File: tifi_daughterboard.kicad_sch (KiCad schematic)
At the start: 20 parts, among them J1 SSW-110-23-F-D, J2 SSW-110-23-F-D, J3 SM04B-SRSS-TB(LF)(SN), J4 SSW-103-02-T-S-RA, Q1 BSS138LT1G, U1 SGP40-D-R4, U2 SHT40-AD1B-R3

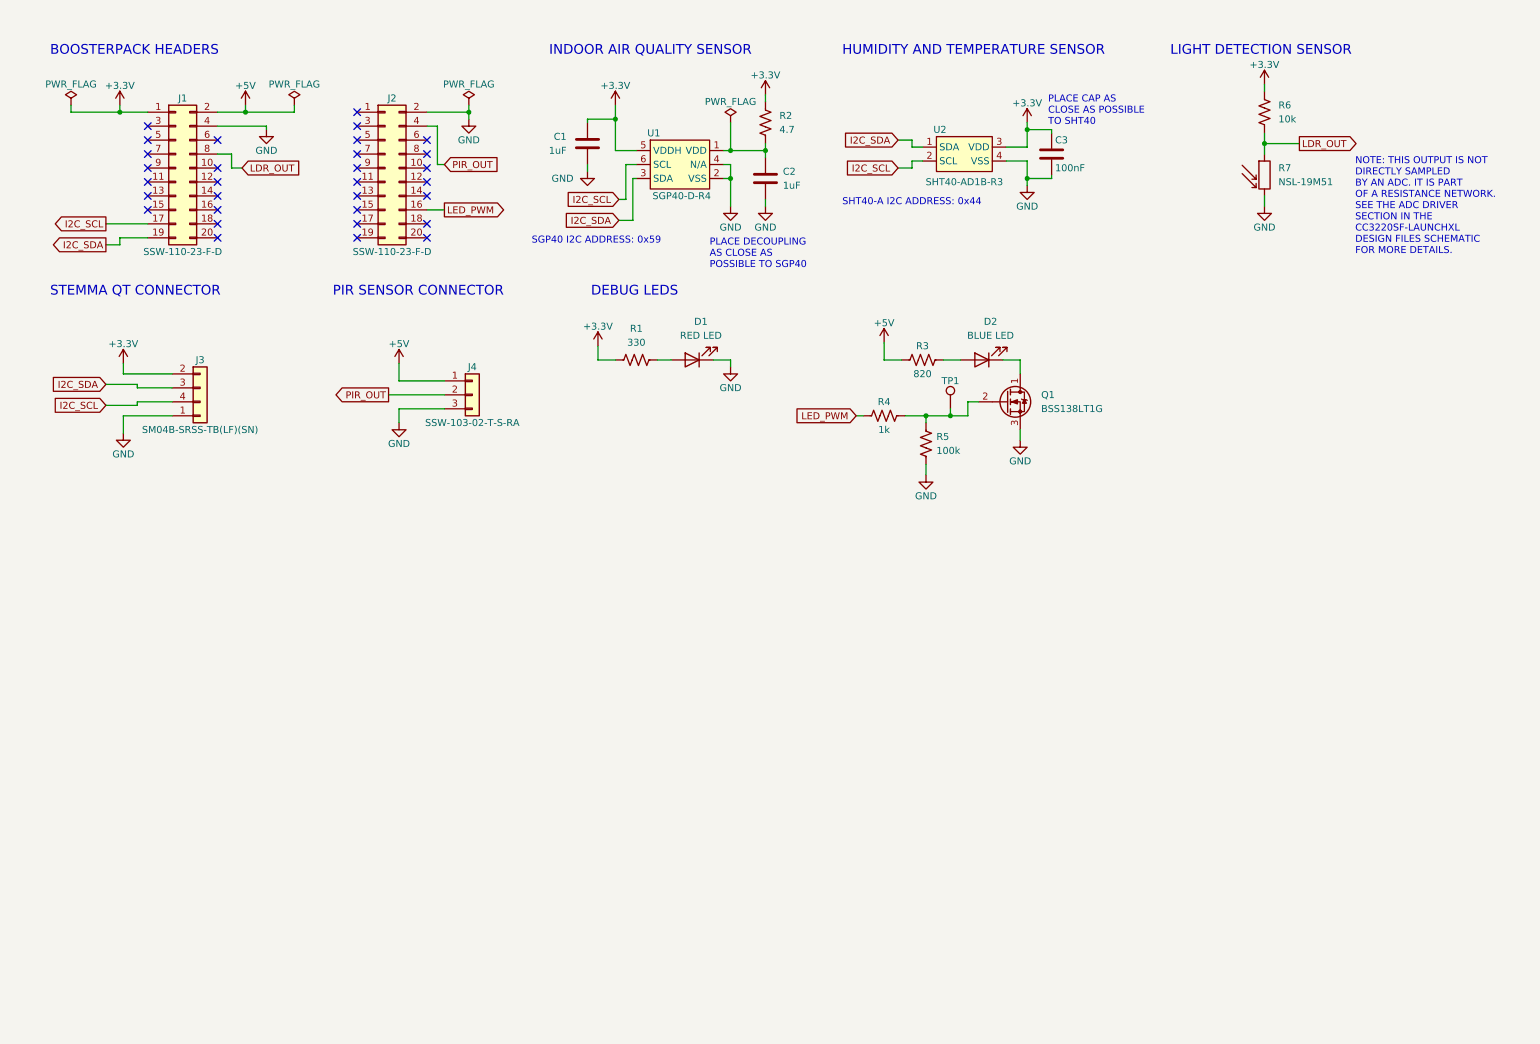
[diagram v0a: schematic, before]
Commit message: Add TVS diodes to connectors.
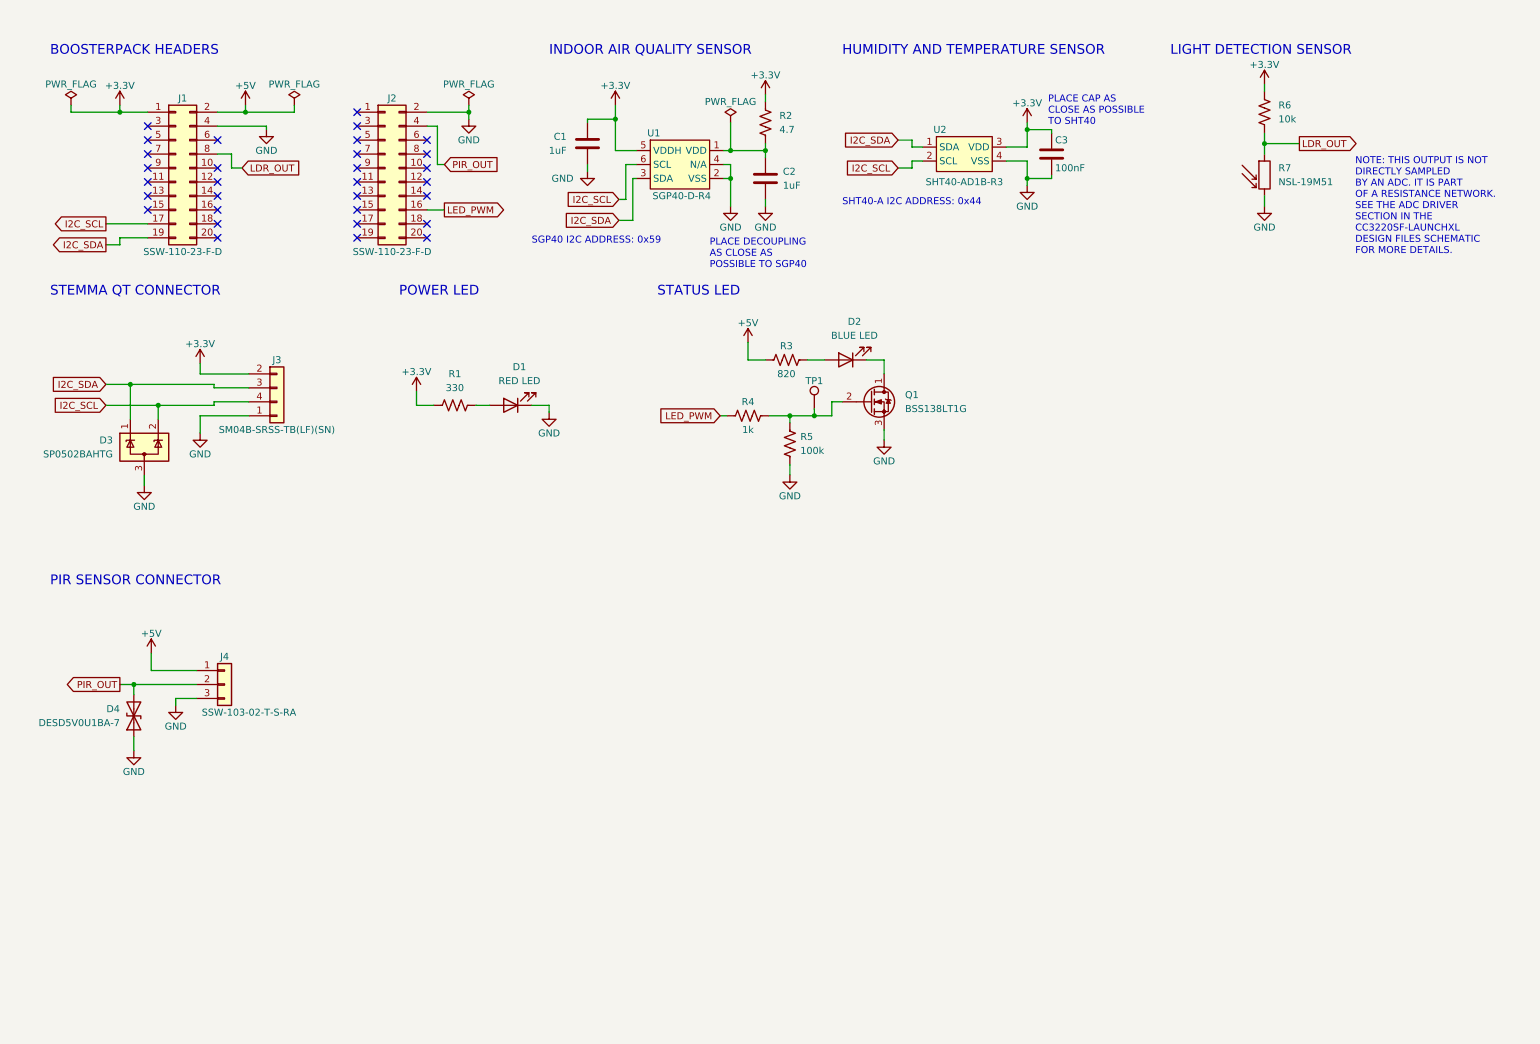
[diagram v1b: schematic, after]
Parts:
- added D3: SP0502BAHTG, Package_TO_SOT_SMD:SOT-23, symbol Power_Protection:SP0502BAHT
- added D4: DESD5V0U1BA-7, TiFi Footprints:D_SOD-323, symbol Device:D_TVS
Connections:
- net GND: now also D3.3 (A), D4.1 (A1)
- net I2C_SCL: now also D3.2 (K)
- net I2C_SDA: now also D3.1 (K)
- net PIR_OUT: now also D4.2 (A2)
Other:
- note added: "POWER LED"
- note added: "STATUS LED"
- note removed: "DEBUG LEDS"
- moved on the sheet: D1, D2, J3, J4, Q1, R1, R3, R4, R5, TP1

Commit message: Add optional I2C pullups.
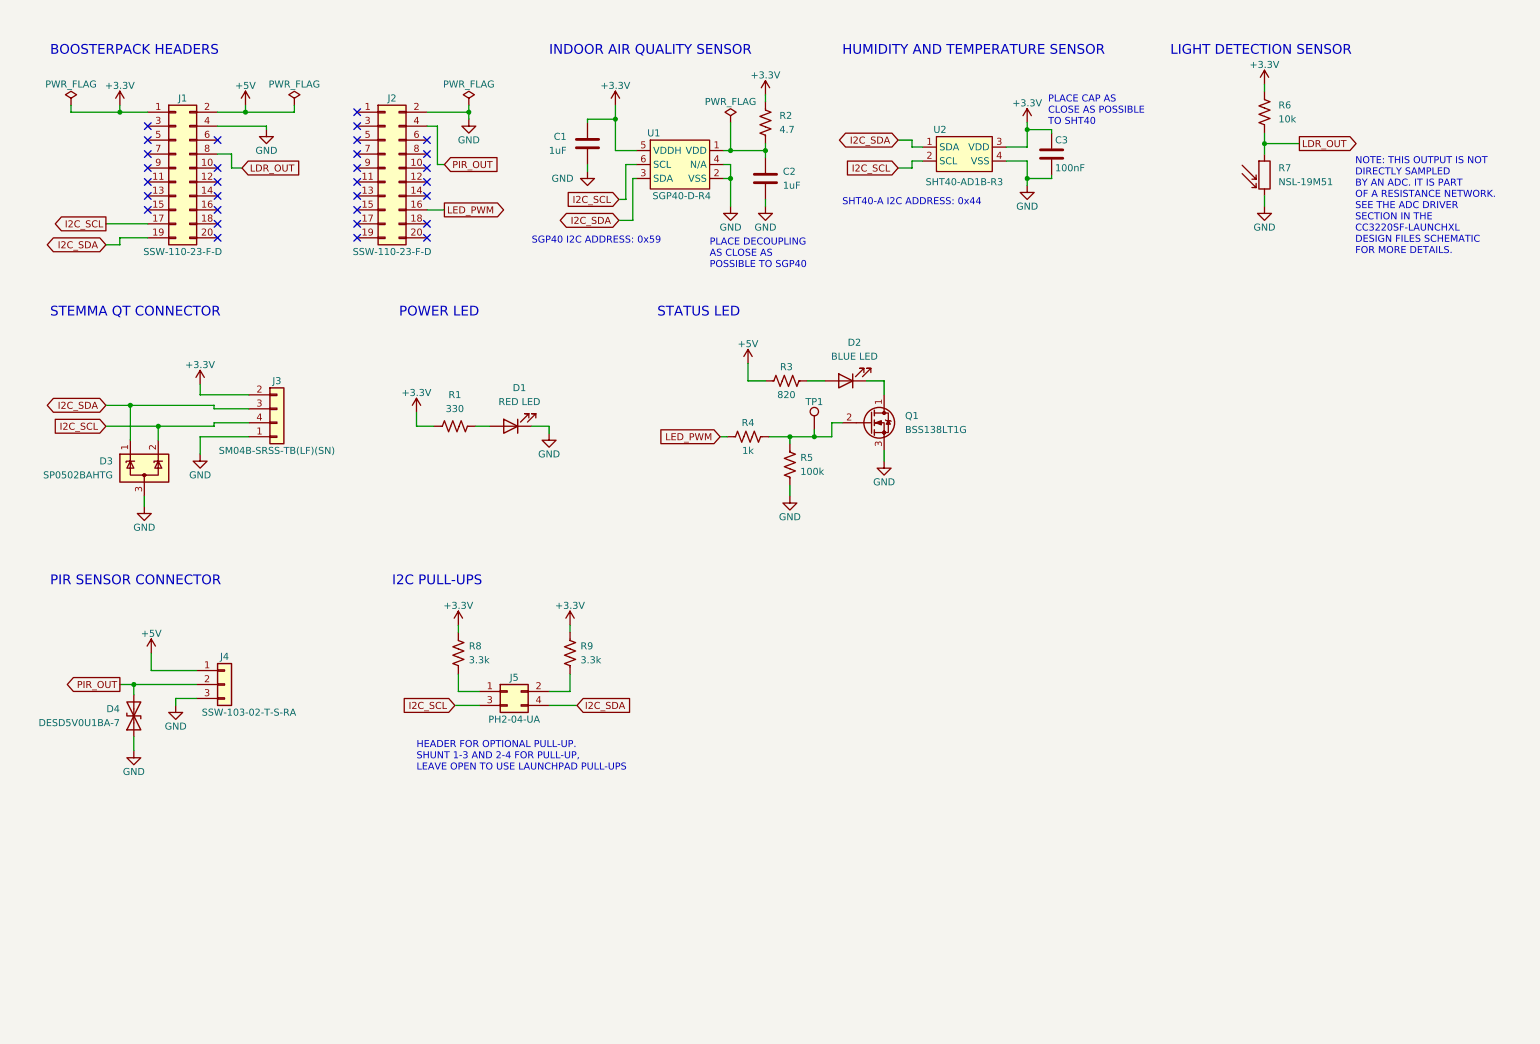
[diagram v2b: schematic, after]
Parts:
- added J5: PH2-04-UA, Connector_PinHeader_2.54mm:PinHeader_2x02_P2.54mm_Vertical, symbol Connector_Generic:Conn_02x02_Odd_Even
- added R8, R9: 3.3k, Resistor_SMD:R_0805_2012Metric, symbol Device:R_US
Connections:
- net +3.3V: now also R8.1, R9.1
- net I2C_SCL: now also J5.3 (Pin_3)
- net I2C_SDA: now also J5.4 (Pin_4)
- new net: J5.1 (Pin_1), R8.2
- new net: J5.2 (Pin_2), R9.2
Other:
- note added: "HEADER FOR OPTIONAL PULL-UP. SHUNT 1-3 AND 2-4 FOR PULL-UP, LEAVE OPEN TO USE LAUNCHPAD PULL-UPS"
- note added: "I2C PULL-UPS"
- moved on the sheet: D1, D2, D3, J3, Q1, R1, R3, R4, R5, TP1

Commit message: Add mask clearance and supplier link fields.
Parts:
- Q1: Supplier Link (none) -> https://www.digikey.com/en/products/detail/onsemi/BSS138LT1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
- TP1: now left out of the parts list
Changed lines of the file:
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@@
   )
   (symbol (lib_id "Connector:TestPoint") (at 158.115 88.265 0) (unit 1)
-    (in_bom yes) (on_board yes)
+    (in_bom no) (on_board yes)
     (property "Reference" "TP1" (id 0) (at 158.115 83.185 0))
     (property "Value" "TestPoint" (id 1) (at 158.115 83.185 0)
@@
       (effects (font (size 1.27 1.27)) hide)
     )
+    (property "Supplier Link" "https://www.digikey.com/en/products/detail/onsemi/BSS138LT1G/918376" (id 4) (at 168.275 86.995 0)
+      (effects (font (size 1.27 1.27)) hide)
+    )

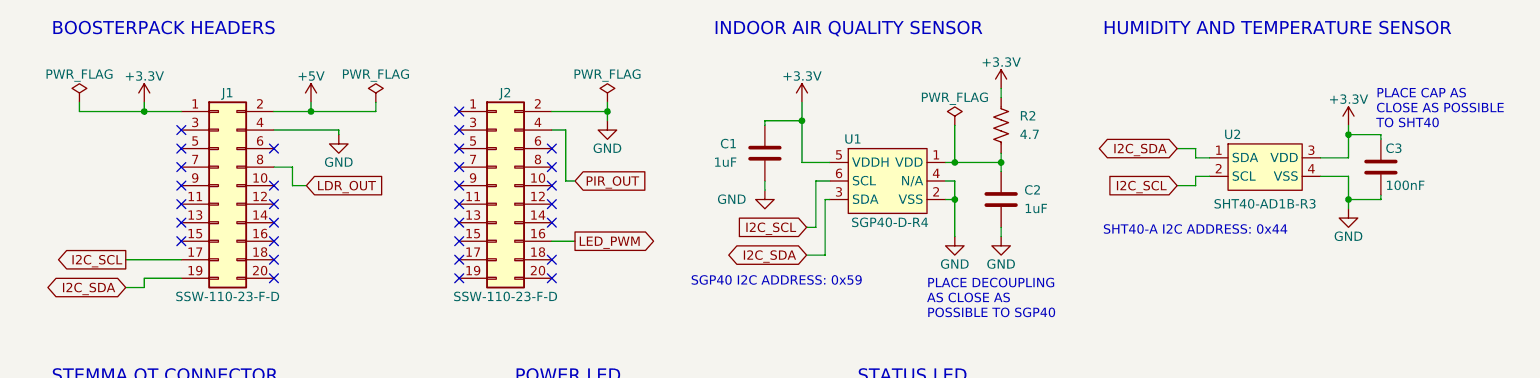
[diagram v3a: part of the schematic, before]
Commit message: Add bulk capacitors to schmatic and board.
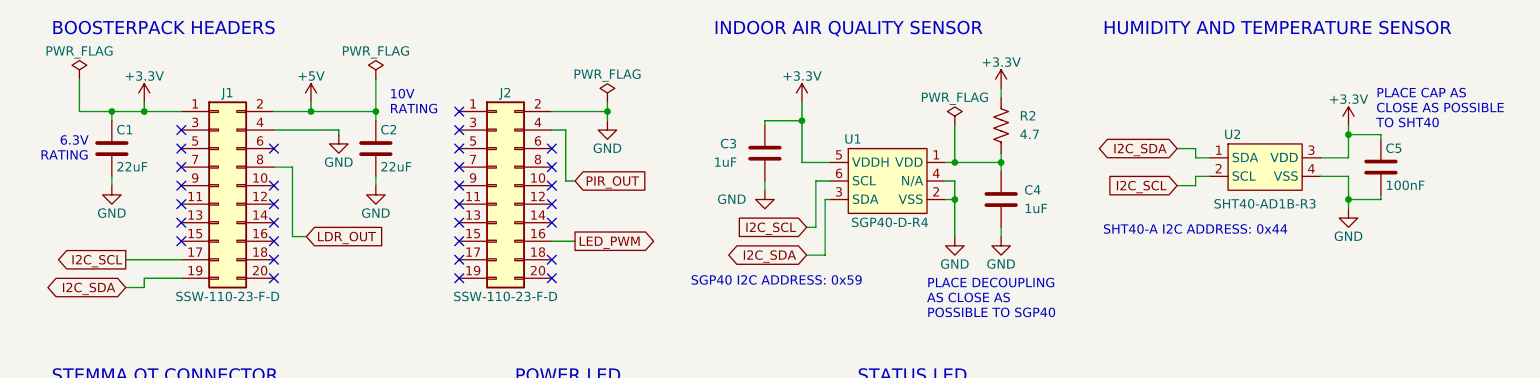
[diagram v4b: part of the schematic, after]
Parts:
- added C1, C2: 22uF, Capacitor_SMD:C_1206_3216Metric, symbol Device:C
- renumbered C1 to C3, C2 to C4, C3 to C5
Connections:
- net +3.3V: now also C1.1
- net +5V: now also C2.1
- net GND: now also C1.2, C2.2
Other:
- note added: "10V RATING"
- note added: "6.3V RATING"

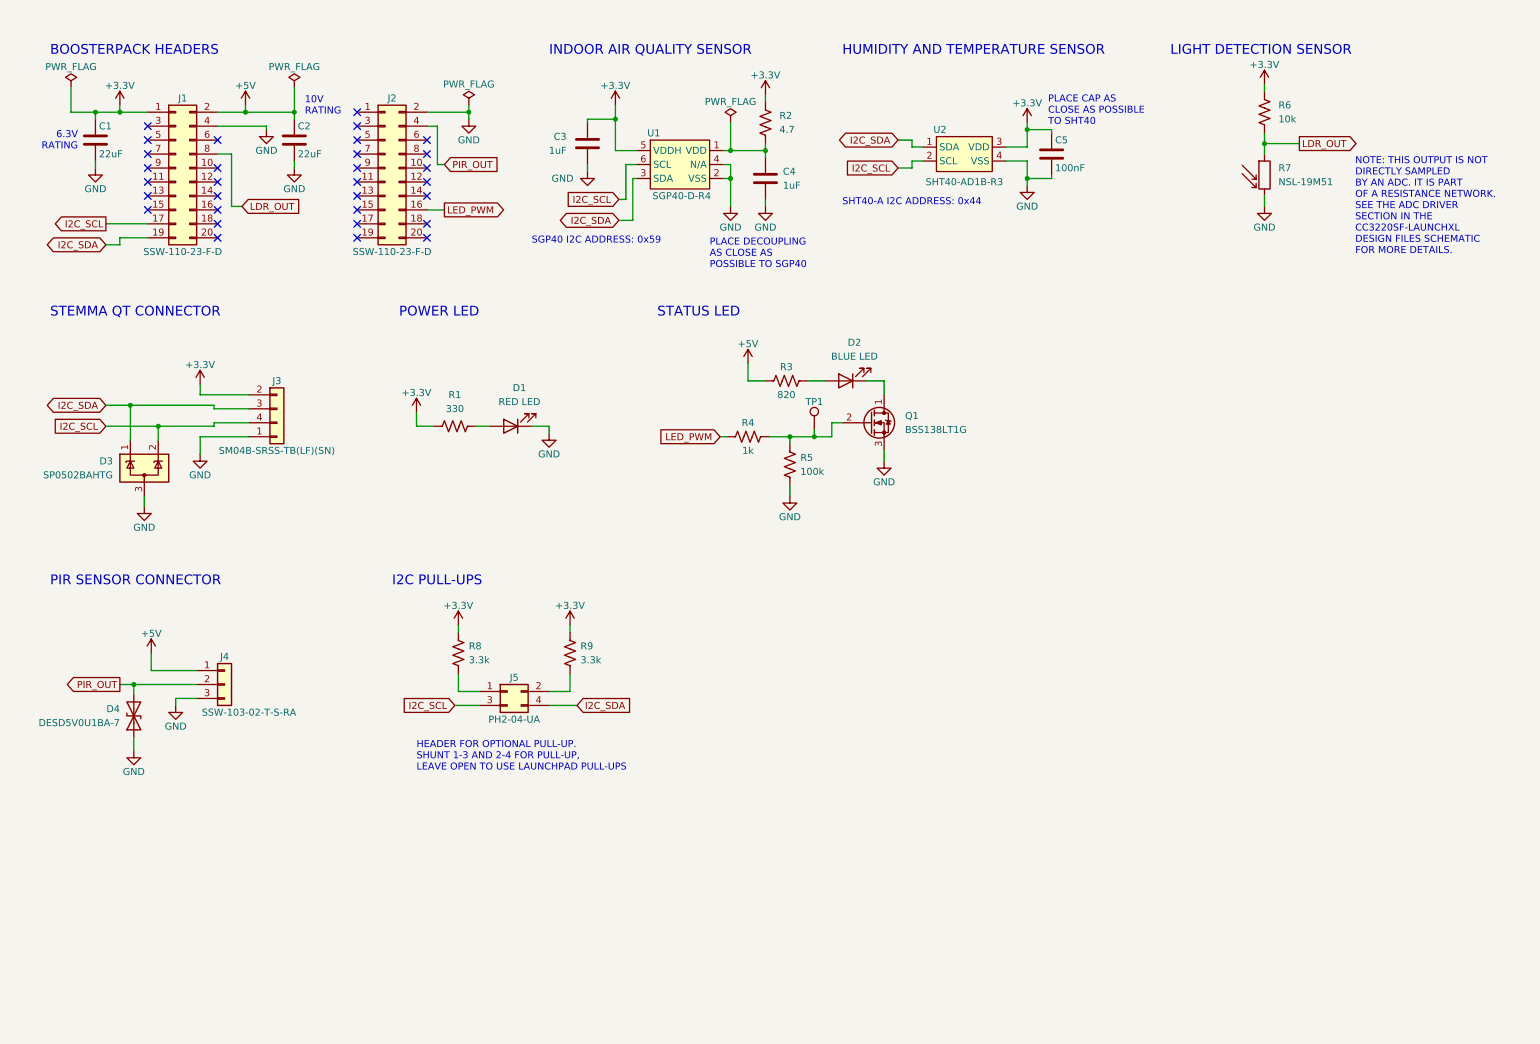
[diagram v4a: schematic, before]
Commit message: Add board fiducials and pad to SGP40 symbol.
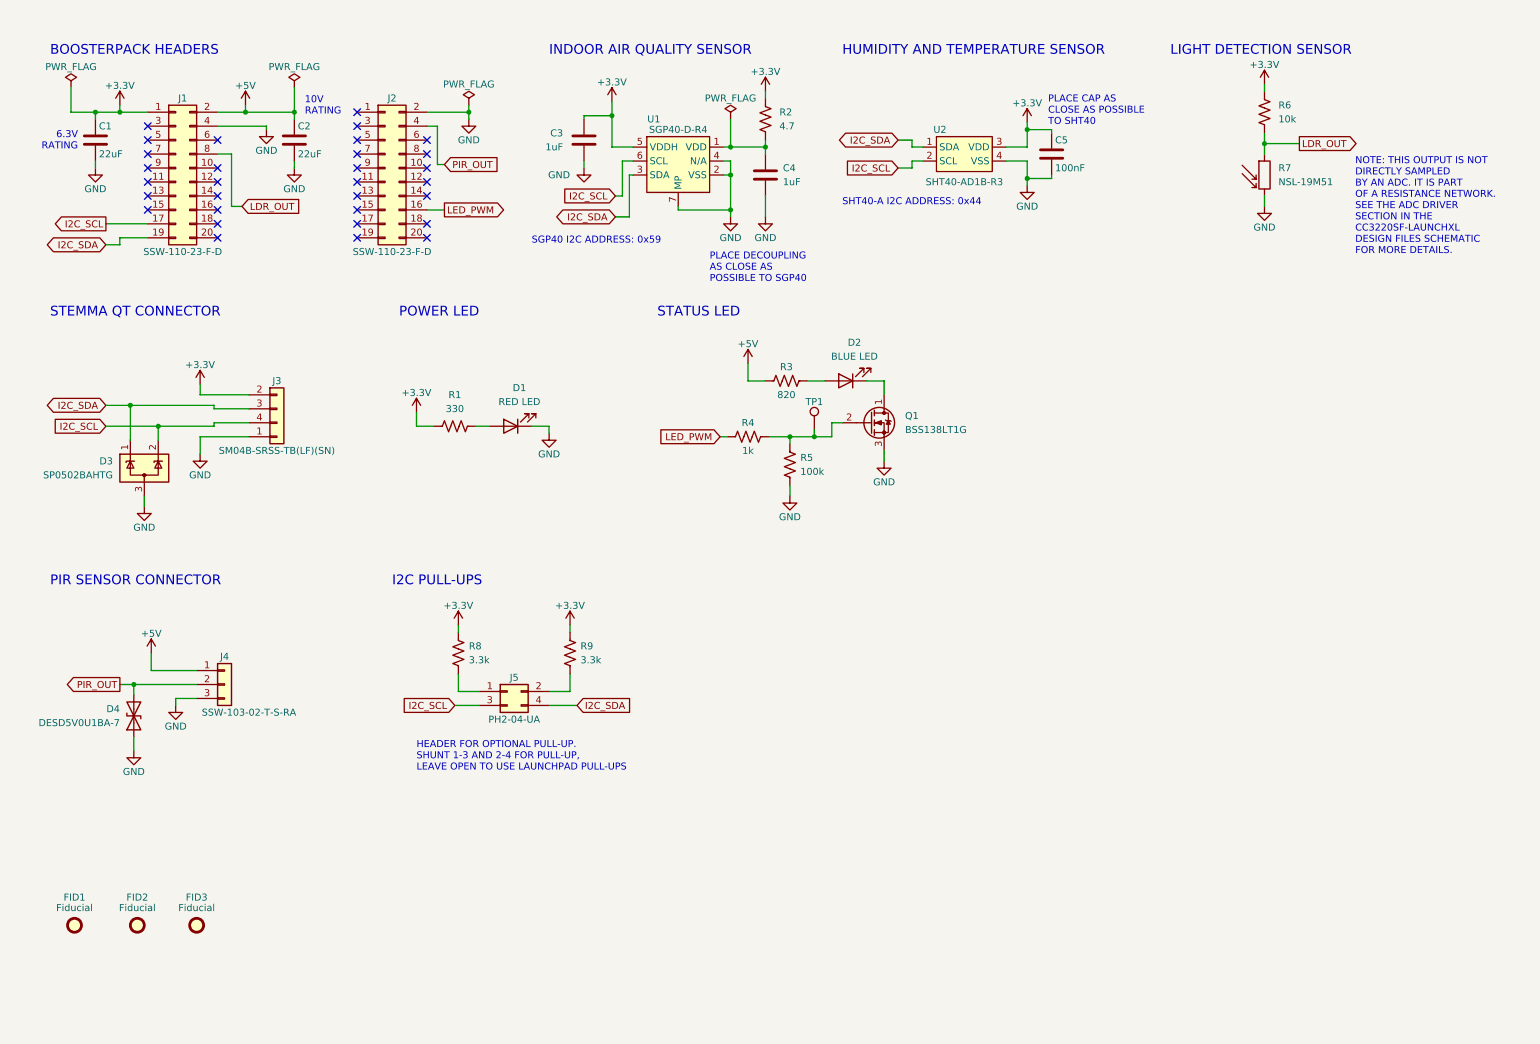
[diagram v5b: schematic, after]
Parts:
- added FID1, FID2, FID3: Fiducial, Fiducial:Fiducial_1mm_Mask2mm, symbol Mechanical:Fiducial
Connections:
- net GND: now also U1.7 (MP)
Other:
- moved on the sheet: C3, C4, R2
